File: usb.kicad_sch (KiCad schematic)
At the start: 8 parts

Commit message: Worked on ETH
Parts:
- D1: footprint (none) -> Diode_SMD:D_SMA
- gave numbers to parts that had none: 5
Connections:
- net VBUS: now also D1.2 (A), D2.1 (A1), J2.A4 (VBUS), J2.A9 (VBUS), J2.B4 (VBUS), J2.B9 (VBUS), U3.5; no longer D1.1 (K)
- new net 4V: D1.1 (K)
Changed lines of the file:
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@@
+		)
+	)
+	(label "VBUS"
+		(at 107.95 55.88 0)
+		(effects
+			(font
+				(size 1.27 1.27)
+			)
+			(justify left bottom)
 		)
 	)
@@
 		(on_board yes)
 		(dnp no)
-		(property "Reference" "C?"
+		(property "Reference" "C1"
 			(at 102.87 140.208 90)
 			(effects
@@
 			(project "miniServer"
 				(path "/2f7e2d6e-7ac1-4ae5-be0e-a6d141d8b943/4ff21490-abe2-4820-a70f-93369b0f595c"
-					(reference "C?")
+					(reference "C1")
 					(unit 1)
 				)
@@
 		(on_board yes)
 		(dnp no)
-		(property "Reference" "R?"
+		(property "Reference" "R3"
 			(at 102.87 129.54 90)
 			(effects
@@
 			(project "miniServer"
 				(path "/2f7e2d6e-7ac1-4ae5-be0e-a6d141d8b943/4ff21490-abe2-4820-a70f-93369b0f595c"
-					(reference "R?")
+					(reference "R3")
 					(unit 1)
 				)
@@
 			)
 		)
-		(property "Footprint" ""
+		(property "Footprint" "Diode_SMD:D_SMA"
 			(at 125.73 45.72 0)
 			(effects
@@
 		(on_board yes)
 		(dnp no)
-		(property "Reference" "U?"
+		(property "Reference" "U3"
 			(at 76.708 62.484 90)
 			(effects
@@
 			(project "miniServer"
 				(path "/2f7e2d6e-7ac1-4ae5-be0e-a6d141d8b943/4ff21490-abe2-4820-a70f-93369b0f595c"
-					(reference "U?")
+					(reference "U3")
 					(unit 1)
 				)
@@
 		(dnp no)
 		(fields_autoplaced yes)
-		(property "Reference" "J?"
+		(property "Reference" "J2"
 			(at 99.06 81.28 0)
 			(effects
@@
 			(project "miniServer"
 				(path "/2f7e2d6e-7ac1-4ae5-be0e-a6d141d8b943/4ff21490-abe2-4820-a70f-93369b0f595c"
-					(reference "J?")
+					(reference "J2")
 					(unit 1)
 				)
@@
 		(dnp no)
 		(fields_autoplaced yes)
-		(property "Reference" "#PWR?"
+		(property "Reference" "#PWR0101"
 			(at 99.06 152.4 0)
 			(effects
@@
 			(project "miniServer"
 				(path "/2f7e2d6e-7ac1-4ae5-be0e-a6d141d8b943/4ff21490-abe2-4820-a70f-93369b0f595c"
-					(reference "#PWR?")
+					(reference "#PWR0101")
 					(unit 1)
 				)
@@
 			)
 		)
-		(property "Value" "VBUS"
+		(property "Value" "4V"
 			(at 125.73 33.02 0)
 			(effects
@@
 		(dnp no)
 		(fields_autoplaced yes)
-		(property "Reference" "#PWR?"
+		(property "Reference" "#PWR0102"
 			(at 67.31 87.63 0)
 			(effects
@@
 			(project "miniServer"
 				(path "/2f7e2d6e-7ac1-4ae5-be0e-a6d141d8b943/4ff21490-abe2-4820-a70f-93369b0f595c"
-					(reference "#PWR?")
+					(reference "#PWR0102")
 					(unit 1)
 				)
@@
 		(on_board yes)
 		(dnp no)
-		(property "Reference" "D?"
+		(property "Reference" "D2"
 			(at 131.826 65.024 90)
 			(effects
@@
 			(project "miniServer"
 				(path "/2f7e2d6e-7ac1-4ae5-be0e-a6d141d8b943/4ff21490-abe2-4820-a70f-93369b0f595c"
-					(reference "D?")
-					(unit 1)
-				)
+					(reference "D2")
+					(unit 1)
+				)

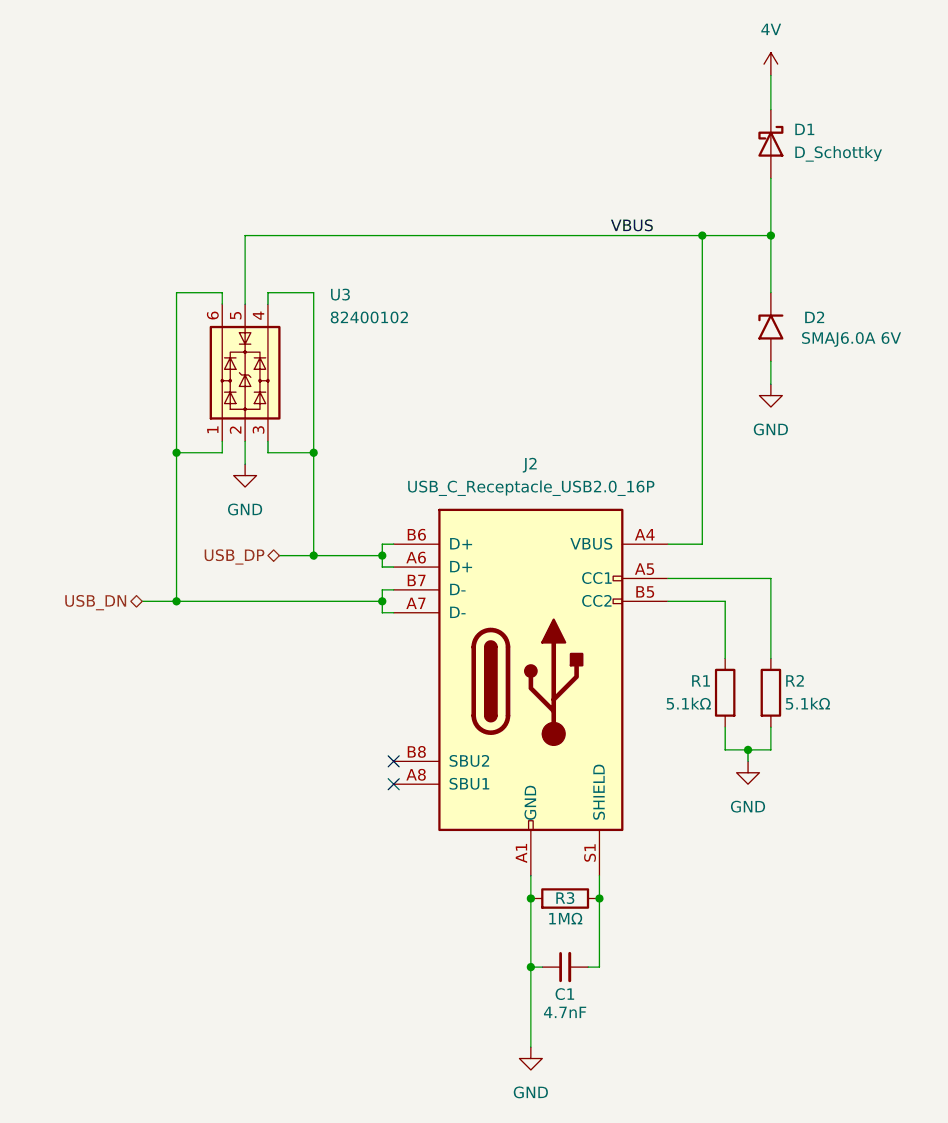
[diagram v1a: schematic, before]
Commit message: Added SDMMC
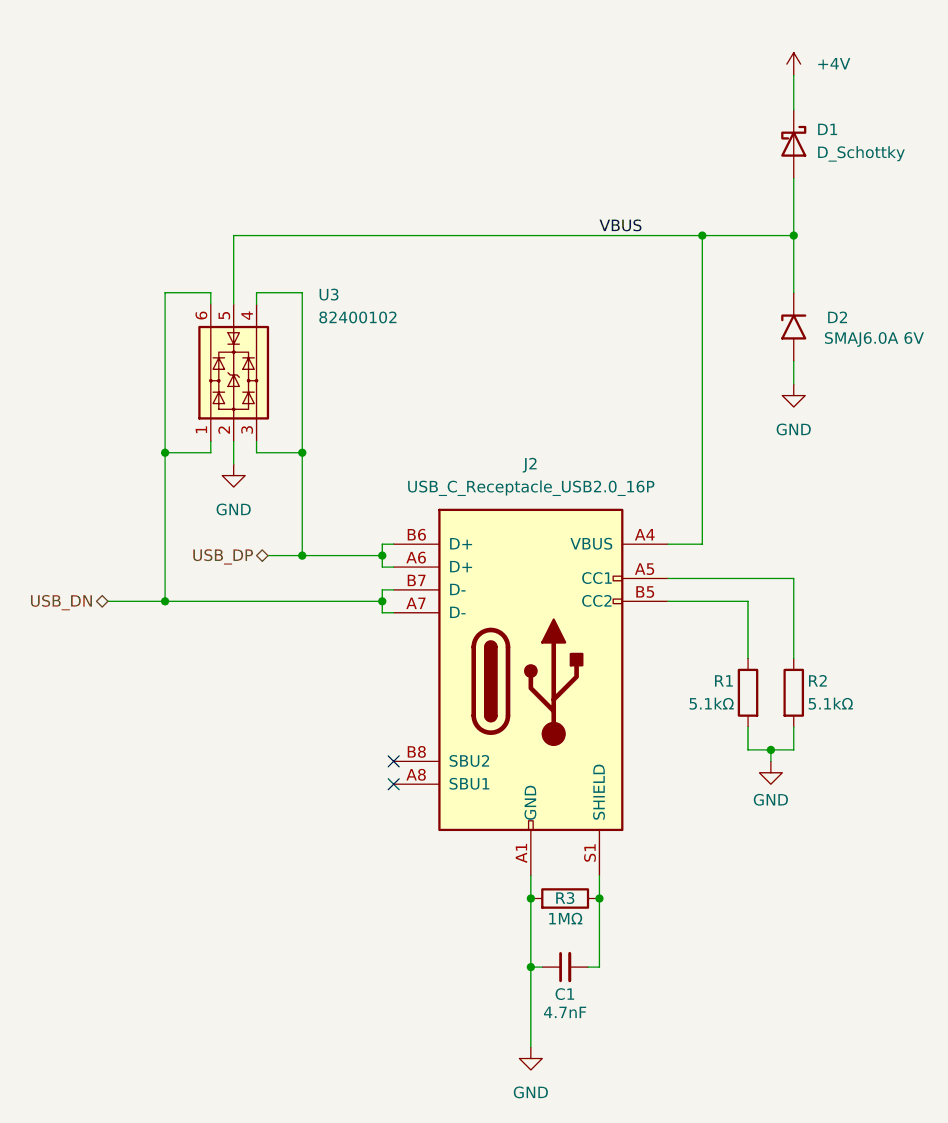
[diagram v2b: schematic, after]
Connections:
- net 4V renamed +4V
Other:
- moved on the sheet: D1, D2, R1, R2, U3
